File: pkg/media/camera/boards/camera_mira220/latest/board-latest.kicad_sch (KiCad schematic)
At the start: 45 parts, among them J2 FPC, U1 TCR3DF25LM, U2 TCR2EF18LM, U3 TCR2EF135LM, U5 LM3880MF-1AA/NOPB, X2 ECS-2520MV-xxx-xx

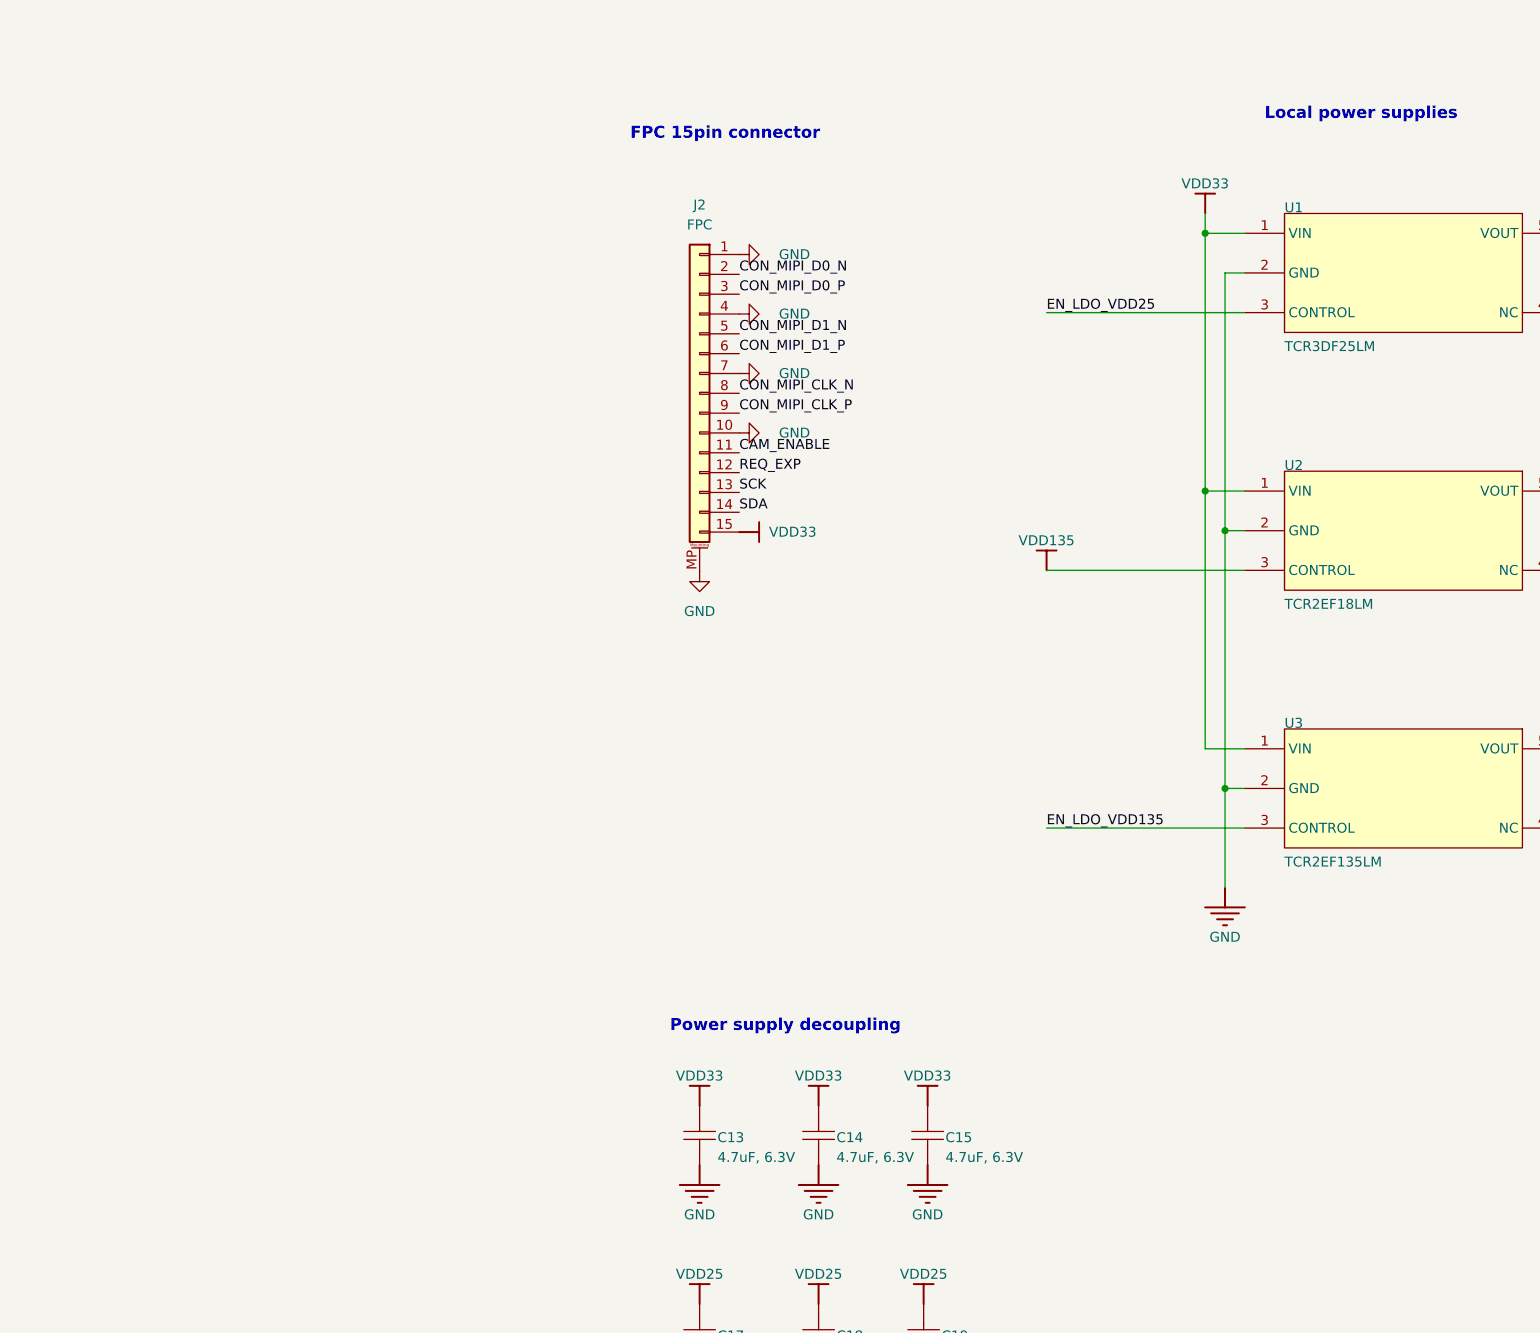
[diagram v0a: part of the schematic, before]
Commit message: Adding more recent changes and improving licensing.
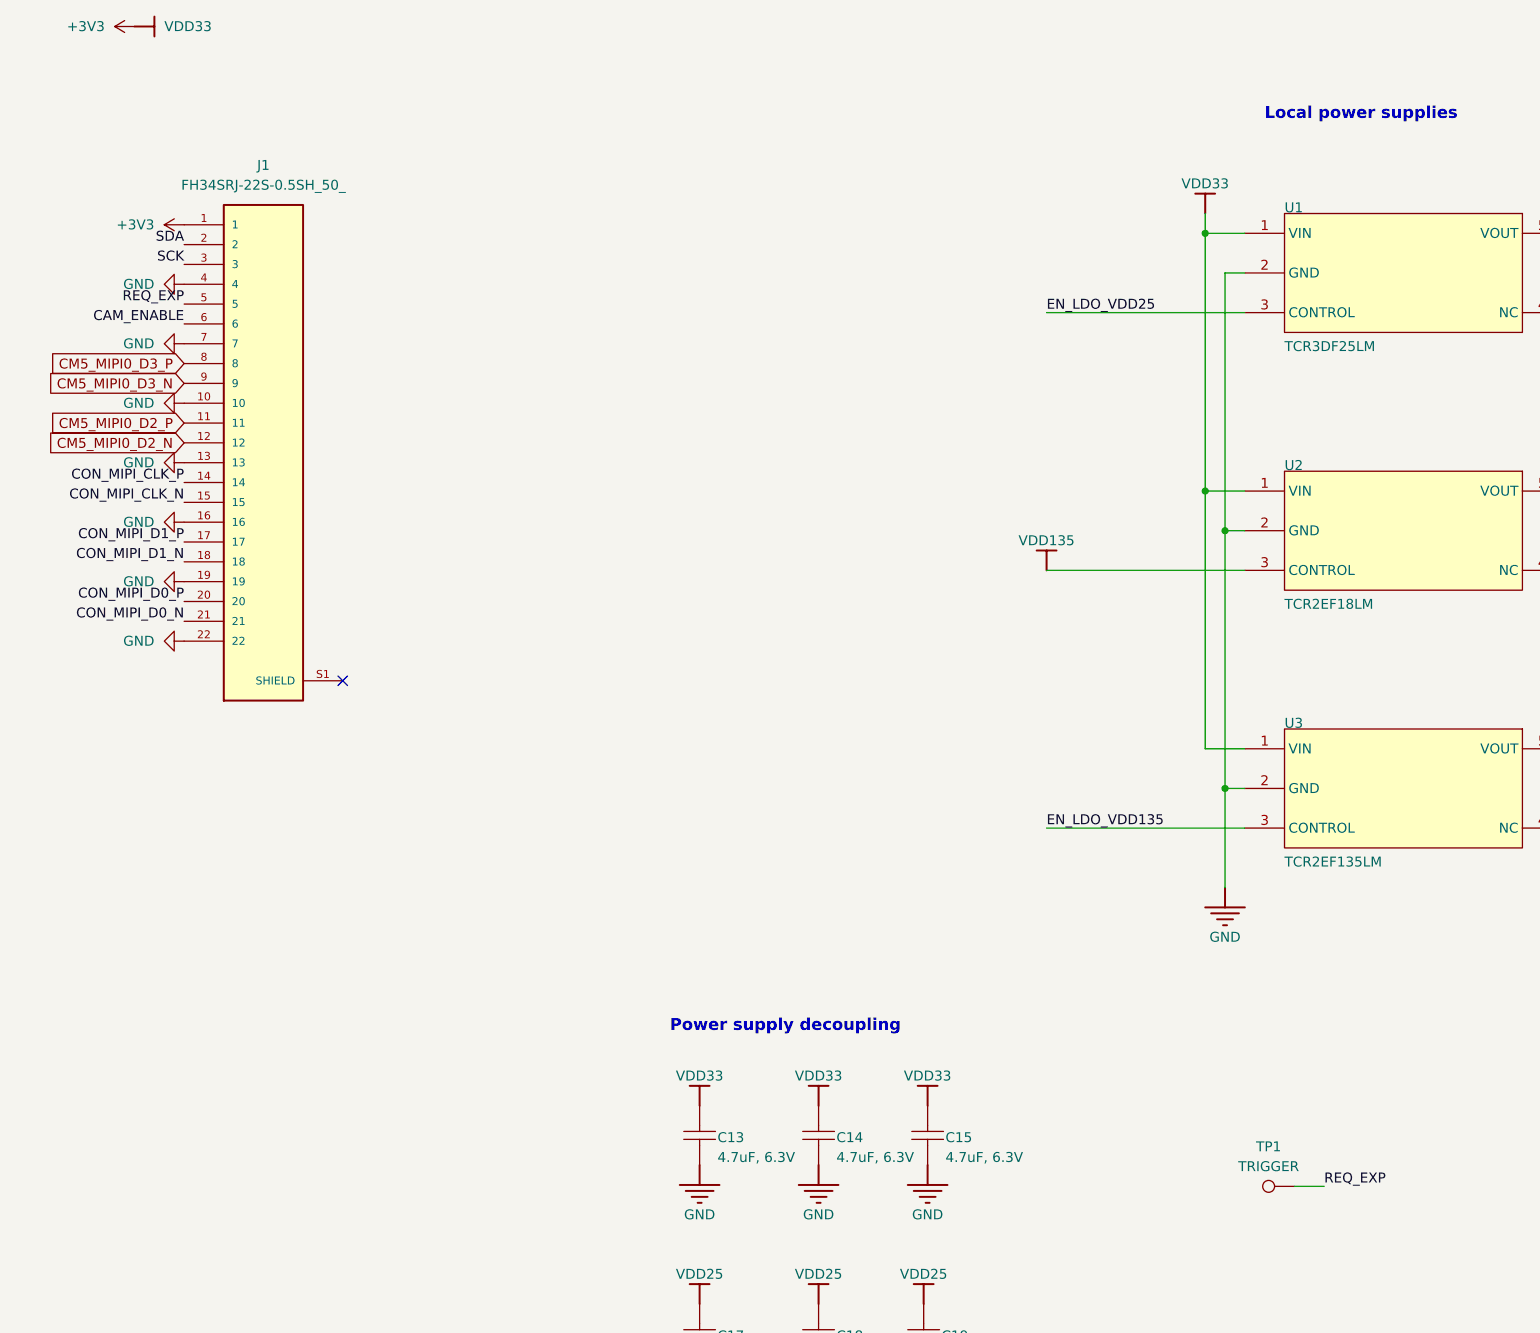
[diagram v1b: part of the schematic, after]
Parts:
- removed J2: FPC, Connector_FFC-FPC:TE_1-84952-5_1x15-1MP_P1.0mm_Horizontal, symbol Connector_Generic_MountingPin:Conn_01x15_MountingPin
- added J1: FH34SRJ-22S-0.5SH_50_, FH34SRJ-22S-0.5SH_50_:HRS_FH34SRJ-22S-0.5SH_50_, symbol FH34SRJ-22S-0.5SH_50_:FH34SRJ-22S-0.5SH_50_
- added TP1: TRIGGER, TestPoint:TestPoint_Pad_D1.0mm, symbol Connector:TestPoint
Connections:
- net CAM_ENABLE: now also J1.6
- net CON_MIPI_CLK_N: now also J1.15
- net CON_MIPI_CLK_P: now also J1.14
- net CON_MIPI_D0_N: now also J1.21
- net CON_MIPI_D0_P: now also J1.20
- net CON_MIPI_D1_N: now also J1.18
- net CON_MIPI_D1_P: now also J1.17
- net GND: now also J1.10, J1.13, J1.16, J1.19, J1.22, J1.4, J1.7
- net REQ_EXP: now also J1.5, TP1.1
- net SCK: now also J1.3
- net SDA: now also J1.2
- net VDD33 renamed +3V3
- net +3V3: now also J1.1
- new net: J1.S1 (SHIELD), J1.S2 (SHIELD)
- new net CM5_MIPI0_D2_N: J1.12
- new net CM5_MIPI0_D2_P: J1.11
- new net CM5_MIPI0_D3_N: J1.9
- new net CM5_MIPI0_D3_P: J1.8
- no-connect marks 8 -> 9
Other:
- note removed: "FPC 15pin connector"

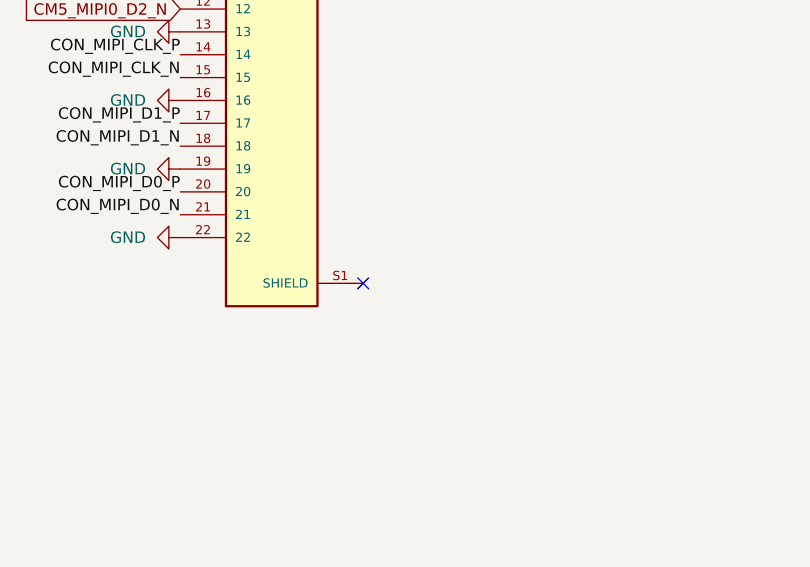
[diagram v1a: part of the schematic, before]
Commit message: Adding more cnc logging logic.
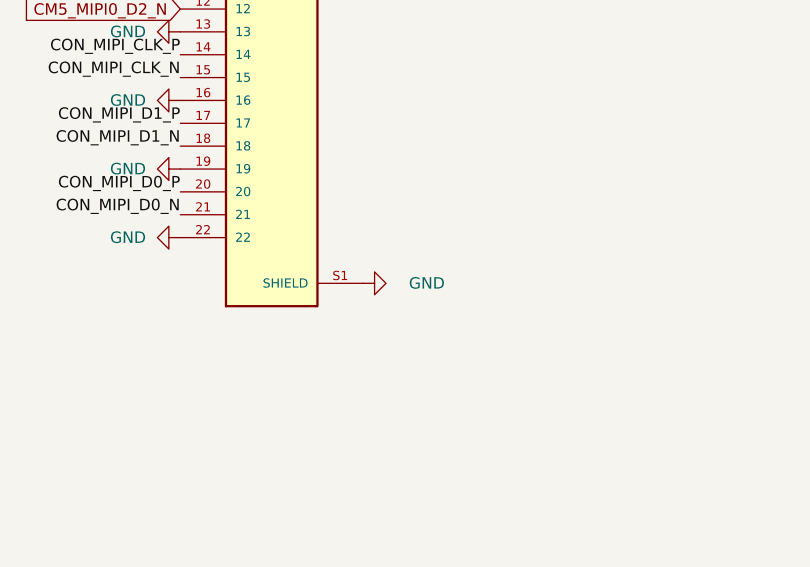
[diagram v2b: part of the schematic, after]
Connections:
- net GND: now also J1.S1 (SHIELD), J1.S2 (SHIELD)
- no-connect marks 9 -> 8
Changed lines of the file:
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@@
 	)
 	(no_connect
-		(at -15.24 92.71)
-	)
-	(no_connect
 		(at 370.84 130.6322)
 	)
@@
 					(unit 1)
 				)
+			)
+		)
+	)
+	(symbol
+		(lib_id "power:GND")
+		(at -15.24 92.71 90)
+		(unit 1)
+		(exclude_from_sim no)
+		(in_bom yes)
+		(on_board yes)
+		(dnp no)
+		(fields_autoplaced yes)
+		(property "Reference" "#PWR01"
+			(at -8.89 92.71 0)
+			(effects
+				(font
+					(size 1.27 1.27)
+				)
+				(hide yes)
+			)
+		)
+		(property "Value" "GND"
+			(at -10.16 92.7099 90)
+			(effects
+				(font
+					(size 1.27 1.27)
+				)
+				(justify right)
+			)
+		)
+		(property "Footprint" ""
+			(at -15.24 92.71 0)
+			(effects
+				(font
+					(size 1.27 1.27)
+				)
+				(hide yes)
+			)
+		)
+		(property "Datasheet" ""
+			(at -15.24 92.71 0)
+			(effects
+				(font
+					(size 1.27 1.27)
+				)
+				(hide yes)
+			)
+		)
+		(property "Description" "Power symbol creates a global label with name \"GND\" , ground"
+			(at -15.24 92.71 0)
+			(effects
+				(font
+					(size 1.27 1.27)
+				)
+				(hide yes)
+			)
+		)
+		(pin "1"
+		)
+		(instances
+			(project "board-latest"
+				(path "/b512ffec-4263-4c79-9981-b486142613ed"
+					(reference "#PWR01")
+					(unit 1)
+				)

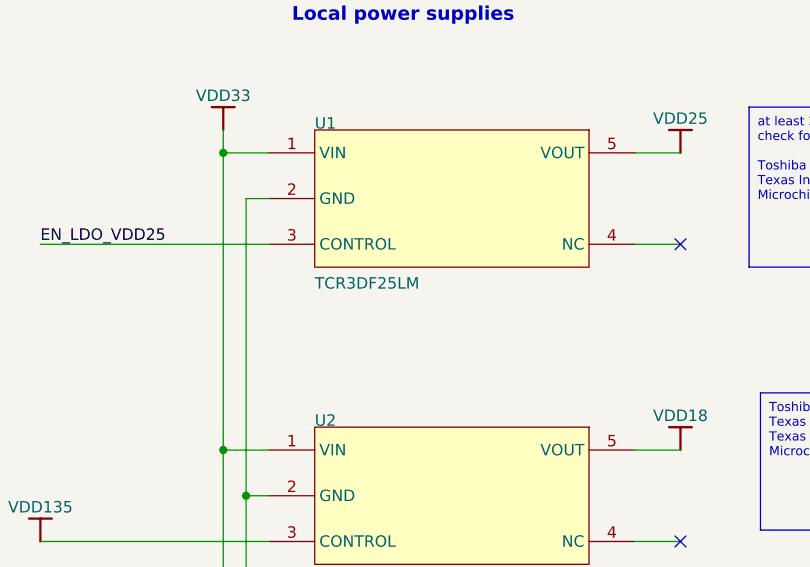
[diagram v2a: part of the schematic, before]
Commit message: Mocap tweaks and add CM4 support with SDCard.
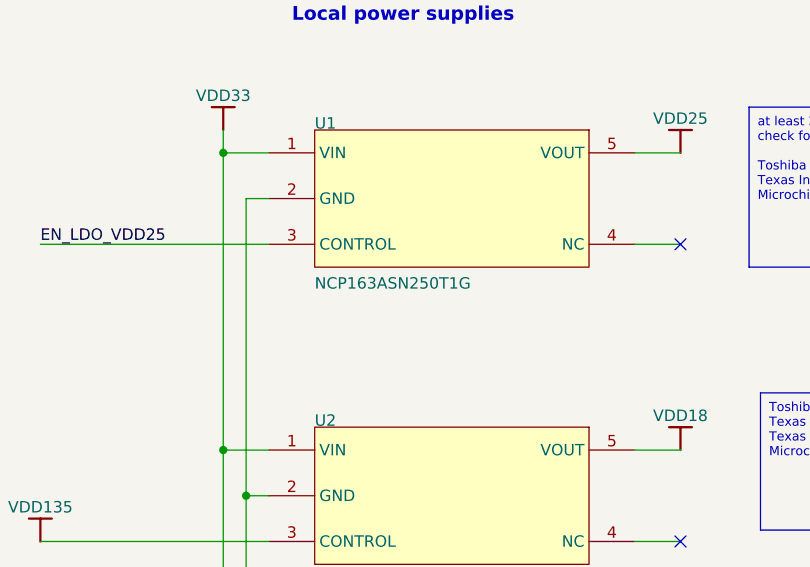
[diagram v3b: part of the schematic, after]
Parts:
- U1: value TCR3DF25LM -> NCP163ASN250T1G
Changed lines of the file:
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@@
 			)
 		)
-		(property "Value" "TCR3DF25LM"
+		(property "Value" "NCP163ASN250T1G"
 			(at 105.41 50.6222 0)
 			(effects
